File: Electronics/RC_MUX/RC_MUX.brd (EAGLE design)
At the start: 33 x 21.6 mm, 24 parts, among them U1 TINY13, U2 MCP1824T, U3 74LS157D

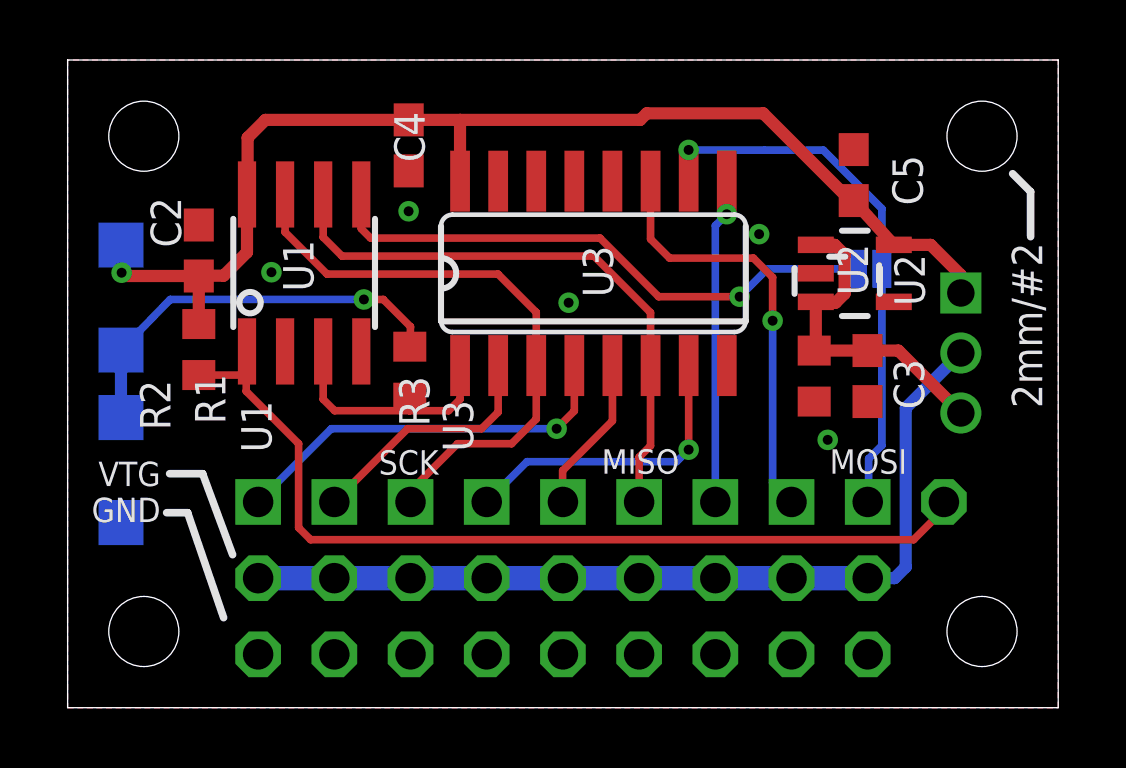
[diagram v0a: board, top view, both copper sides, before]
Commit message: Rev 0.2 as ordered. Widened footprint and changed drill sizes, added labels.
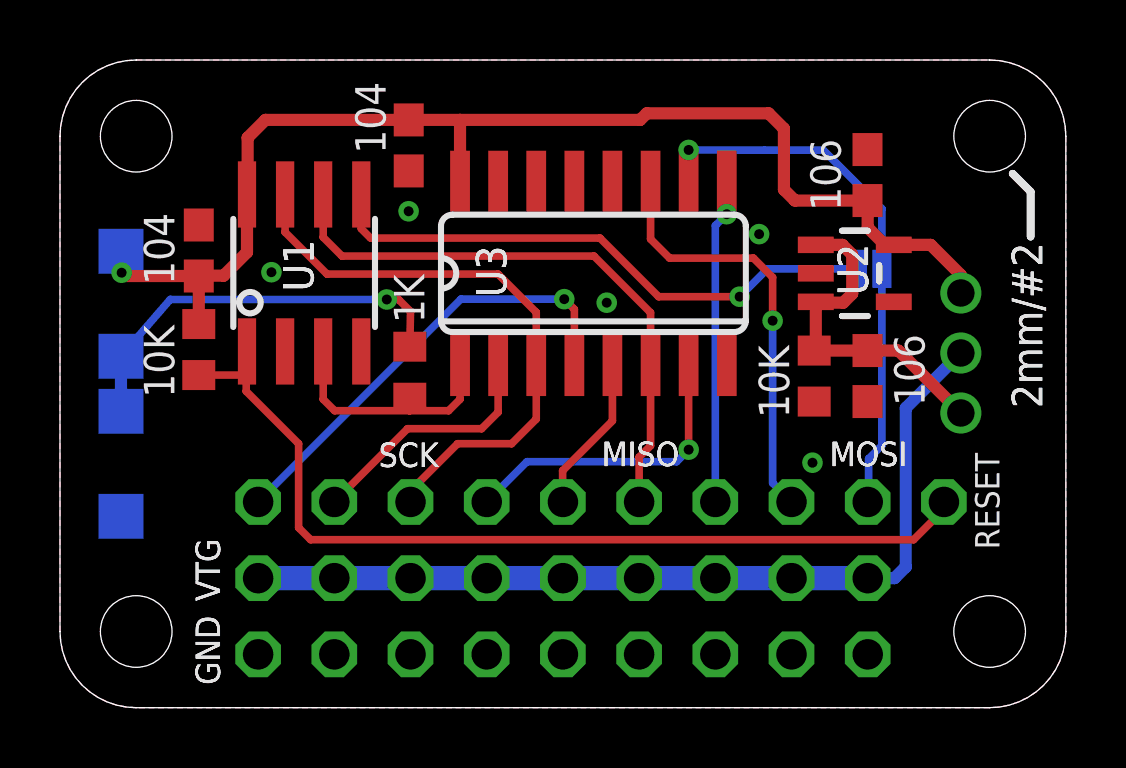
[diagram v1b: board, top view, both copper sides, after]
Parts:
- moved C5 0.46 mm to (26.7, 17.8)
- moved LED1 0.21 mm to (1.78, 13.5)
- moved LED2 0.21 mm to (1.78, 8.13)
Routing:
- net CH1OUT: track 13.3 -> 15.4 mm
- net +5V: track 40.3 -> 41.4 mm
- net REGIN: track 11.3 -> 11.8 mm
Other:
- board size 33 x 21.6 mm -> 33.5 x 21.6 mm
- board text added: "104"
- board text added: "106"
- board text added: "10K"
- board text added: "1K"
- board text added: "1R/C"
- board text added: "2R/C"
- board text added: "3R/C"
- board text added: "MCU"
- board text added: "R/C"
- board text added: "RESET"
- board text removed: "1RX"
- board text removed: "2RX"
- board text removed: "3RX"
- board text removed: "5V | 6V"
- board text removed: "AUTO"
- board text removed: "BOT-THOUGHTS.COM"
- board text removed: "C2"
- board text removed: "C3"
- board text removed: "C4"
- board text removed: "C5"
- board text removed: "MAN"
- board text removed: "R0.1"
- board text removed: "R1"
- board text removed: "R2"
- board text removed: "R3"
- board text removed: "RC MUX"
- board text removed: "SIG>"
